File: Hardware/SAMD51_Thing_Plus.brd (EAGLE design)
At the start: 33 x 58.9 mm, 53 parts, among them J4 CORTEX_DEBUG_PTH, J5 455-1750-1-ND, Q1 2.5A/30V, U1 MCP73831, U2 ATSAMD51J20A-A, U3 AP2112K-3.3V, U4 RFM69HW, Y1 32.768kHz

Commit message: Post review feedback and engineer checklist
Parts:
- removed JP15: (no value), SparkFun-Connectors:USB-B-MICRO-SMD_V03
- added J6: (no value), SparkFun-Connectors:USB-MICROB-PTH-MILL
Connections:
- removed net SHIELD: JP15.SHIELD1, JP15.SHIELD2, JP15.SHIELD3
- net D+: now also J6.D+; no longer JP15.D+
- net D-: now also J6.D-; no longer JP15.D-
- net GND: now also J6.GND; no longer JP15.GND
- net VUSB-RAW: now also J6.VBUS; no longer JP15.VBUS
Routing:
- net VUSB-RAW: track 36.7 -> 38.3 mm
- net V_BATT: track 48.4 -> 49.2 mm
- net D+: track 46.3 -> 46.9 mm
- net D-: track 46.4 -> 46.9 mm
- removed copper zone on layer 1, net SHIELD
- removed copper zone on layer 16, net SHIELD
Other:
- board text added: "ANT"
- board text added: "QWIIC"
- board text added: "RESET"
- board text added: "Units in inches"
- board text removed: "LED5"

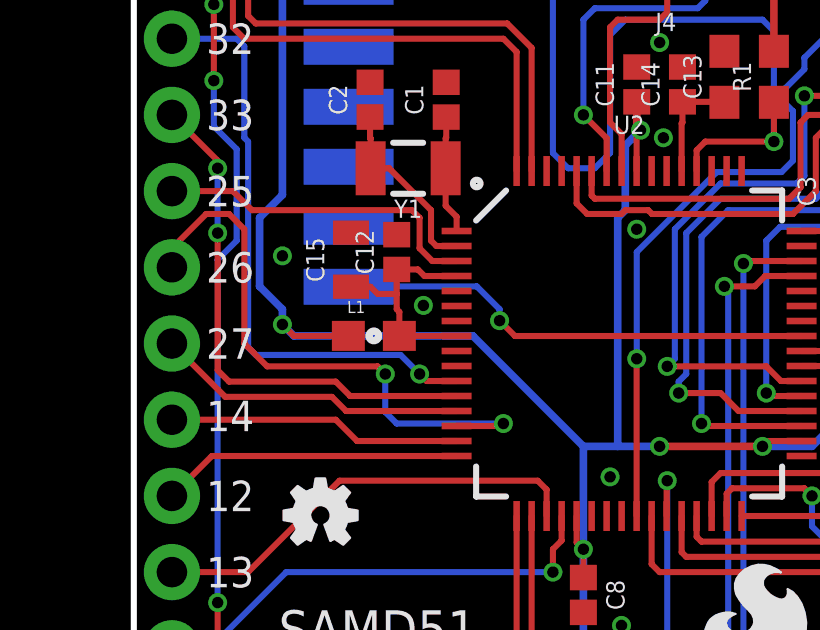
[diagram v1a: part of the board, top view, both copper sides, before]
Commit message: Fixes from QC review
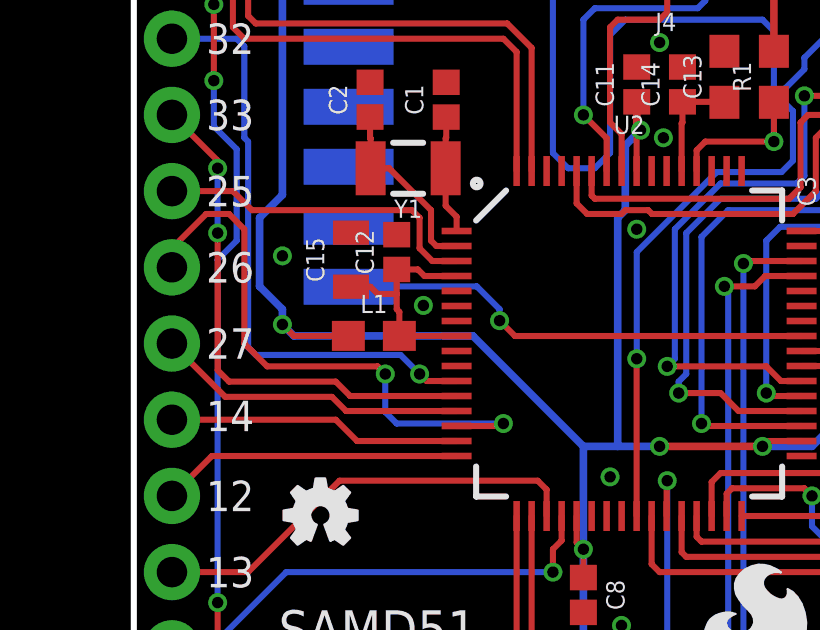
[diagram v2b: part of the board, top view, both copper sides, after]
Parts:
- L1: device SparkFun-Passives:0603 -> SparkFun-Coils:0603
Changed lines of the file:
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@@
 <layer number="20" name="Dimension" color="15" fill="1" visible="yes" active="yes"/>
 <layer number="21" name="tPlace" color="16" fill="1" visible="yes" active="yes"/>
-<layer number="22" name="bPlace" color="14" fill="1" visible="no" active="yes"/>
+<layer number="22" name="bPlace" color="14" fill="1" visible="yes" active="yes"/>
 <layer number="23" name="tOrigins" color="15" fill="1" visible="yes" active="yes"/>
-<layer number="24" name="bOrigins" color="15" fill="1" visible="no" active="yes"/>
-<layer number="25" name="tNames" color="7" fill="1" visible="yes" active="yes"/>
+<layer number="24" name="bOrigins" color="15" fill="1" visible="yes" active="yes"/>
+<layer number="25" name="tNames" color="7" fill="1" visible="no" active="yes"/>
 <layer number="26" name="bNames" color="7" fill="1" visible="no" active="yes"/>
 <layer number="27" name="tValues" color="7" fill="1" visible="no" active="yes"/>
@@
 <layer number="43" name="vRestrict" color="2" fill="10" visible="no" active="yes"/>
 <layer number="44" name="Drills" color="7" fill="1" visible="no" active="yes"/>
-<layer number="45" name="Holes" color="7" fill="1" visible="no" active="yes"/>
+<layer number="45" name="Holes" color="7" fill="1" visible="yes" active="yes"/>
 <layer number="46" name="Milling" color="3" fill="1" visible="no" active="yes"/>
 <layer number="47" name="Measures" color="7" fill="1" visible="no" active="yes"/>
 <layer number="48" name="Document" color="7" fill="1" visible="no" active="yes"/>
 <layer number="49" name="Reference" color="7" fill="1" visible="no" active="yes"/>
-<layer number="51" name="tDocu" color="6" fill="1" visible="no" active="yes"/>
+<layer number="51" name="tDocu" color="6" fill="1" visible="yes" active="yes"/>
 <layer number="52" name="bDocu" color="7" fill="1" visible="no" active="yes"/>
 <layer number="3" name="Route3" color="4" fill="3" visible="no" active="no"/>
@@
 <attribute name="PROD_ID" value="CAP-12416" x="12.954" y="42.926" size="1.778" layer="27" font="vector" ratio="15" rot="R90" display="off"/>
 </element>
-<element name="L1" library="SparkFun-Passives" package="0603" value="FB - 30Ohm" x="8.001" y="34.544">
-<attribute name="PROD_ID" value="RES-07859" x="8.001" y="38.354" size="1.778" layer="27" font="vector" ratio="15" display="off"/>
+<element name="L1" library="SparkFun-Coils" package="0603" value="FB - 30Ohm" x="8.001" y="34.544">
+<attribute name="PROD_ID" value="NDUC-07859" x="8.001" y="38.354" size="1.778" layer="27" font="vector" ratio="15" display="off"/>
 </element>
 <element name="C12" library="SparkFun-Capacitors" package="0402" value="0.1uF" x="8.763" y="37.338" rot="R90">
@@
 </element>
 <element name="LOGO1" library="SparkFun-Aesthetics" package="SFE_LOGO_NAME_FLAME_.2" value="SFE_LOGO_NAME_FLAME.2_INCH" x="5.461" y="16.637"/>
-<element name="J6" library="SparkFun-Connectors" package="USB-MICROB-PTH-MILL" value="" x="7.62" y="2.794"/>
+<element name="J6" library="SparkFun-Connectors" package="USB-MICROB-PTH-MILL" value="" x="7.62" y="2.794">
+<attribute name="PROD_ID" value="CONN-13711" x="7.62" y="2.794" size="1.778" layer="27" display="off"/>
+</element>
 </elements>
 <signals>

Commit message: Replaced retired 1.0uF cap with new one
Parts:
- C7: device SparkFun-Capacitors:0805 -> SparkFun-Capacitors:0603
- J6: value (none) -> AMP FCI 10103594-0001LF; device SparkFun-Connectors:USB-MICROB-PTH-MILL -> SparkFun-Connectors:USB-MICROB-PTH
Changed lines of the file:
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@@
 <attribute name="VALUE" value="6V/0.75A" x="4.445" y="9.525" size="1.778" layer="27" rot="R90" display="off"/>
 </element>
-<element name="C7" library="SparkFun-Capacitors" package="0805" value="1.0uF" x="10.795" y="14.605" rot="R90">
-<attribute name="PROD_ID" value="CAP-11625" x="28.575" y="0.635" size="1.778" layer="27" font="vector" ratio="15" rot="R90" display="off"/>
+<element name="C7" library="SparkFun-Capacitors" package="0603" value="1.0uF" x="10.795" y="14.605" rot="R90">
+<attribute name="PROD_ID" value="CAP-13930" x="28.575" y="0.635" size="1.778" layer="27" font="vector" ratio="15" rot="R90" display="off"/>
 </element>
 <element name="C10" library="SparkFun-Capacitors" package="0603" value="2.2uF" x="4.445" y="14.605" rot="R90">
@@
 </element>
 <element name="LOGO1" library="SparkFun-Aesthetics" package="SFE_LOGO_NAME_FLAME_.2" value="SFE_LOGO_NAME_FLAME.2_INCH" x="5.461" y="16.637"/>
-<element name="J6" library="SparkFun-Connectors" package="USB-MICROB-PTH-MILL" value="" x="7.62" y="2.794">
+<element name="J6" library="SparkFun-Connectors" package="USB-MICROB-PTH" value="AMP FCI 10103594-0001LF" x="7.62" y="2.794">
 <attribute name="PROD_ID" value="CONN-13711" x="7.62" y="2.794" size="1.778" layer="27" display="off"/>
+<attribute name="VALUE" value="AMP FCI 10103594-0001LF" x="7.62" y="2.794" size="1.778" layer="27" display="off"/>
 </element>
 </elements>
@@
 <wire x1="8.9201" y1="13.655" x2="9.779" y2="13.655" width="0.4064" layer="1"/>
 <wire x1="9.779" y1="13.655" x2="10.745" y2="13.655" width="0.4064" layer="1"/>
-<wire x1="10.745" y1="13.655" x2="10.795" y2="13.705" width="0.4064" layer="1"/>
-<wire x1="10.795" y1="13.705" x2="12.285" y2="13.705" width="0.4064" layer="1"/>
+<wire x1="10.745" y1="13.655" x2="10.795" y2="13.755" width="0" layer="19" extent="1-16"/>
 <wire x1="12.285" y1="13.705" x2="12.335" y2="13.655" width="0.4064" layer="1"/>
 <wire x1="12.335" y1="13.655" x2="14.285" y2="13.655" width="0.4064" layer="1"/>
@@
 <wire x1="9.906" y1="15.494" x2="9.906" y2="13.782" width="0.2032" layer="1"/>
 <wire x1="9.906" y1="13.782" x2="9.779" y2="13.655" width="0.2032" layer="1"/>
+<wire x1="12.285" y1="13.705" x2="10.845" y2="13.705" width="0.4064" layer="1"/>
+<wire x1="10.845" y1="13.705" x2="10.795" y2="13.755" width="0.4064" layer="1"/>
 </signal>
 <signal name="N$9">
